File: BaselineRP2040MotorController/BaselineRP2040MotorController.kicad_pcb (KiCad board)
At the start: 2 copper layers, 133 parts, among them J2 Encoder 1, J3 Conn_01x03, J4 XT60 Power Connector, Q1 Q_PNP_BEC, Q2 Q_PNP_BEC, Q3 Q_PNP_BEC, U10 INA240A1D, U11 USBLC6-4SC6, U13 TX4139, U5 EG3113, U6 INA240A1D, U7 EG3113, U8 INA240A1D, U9 EG3113

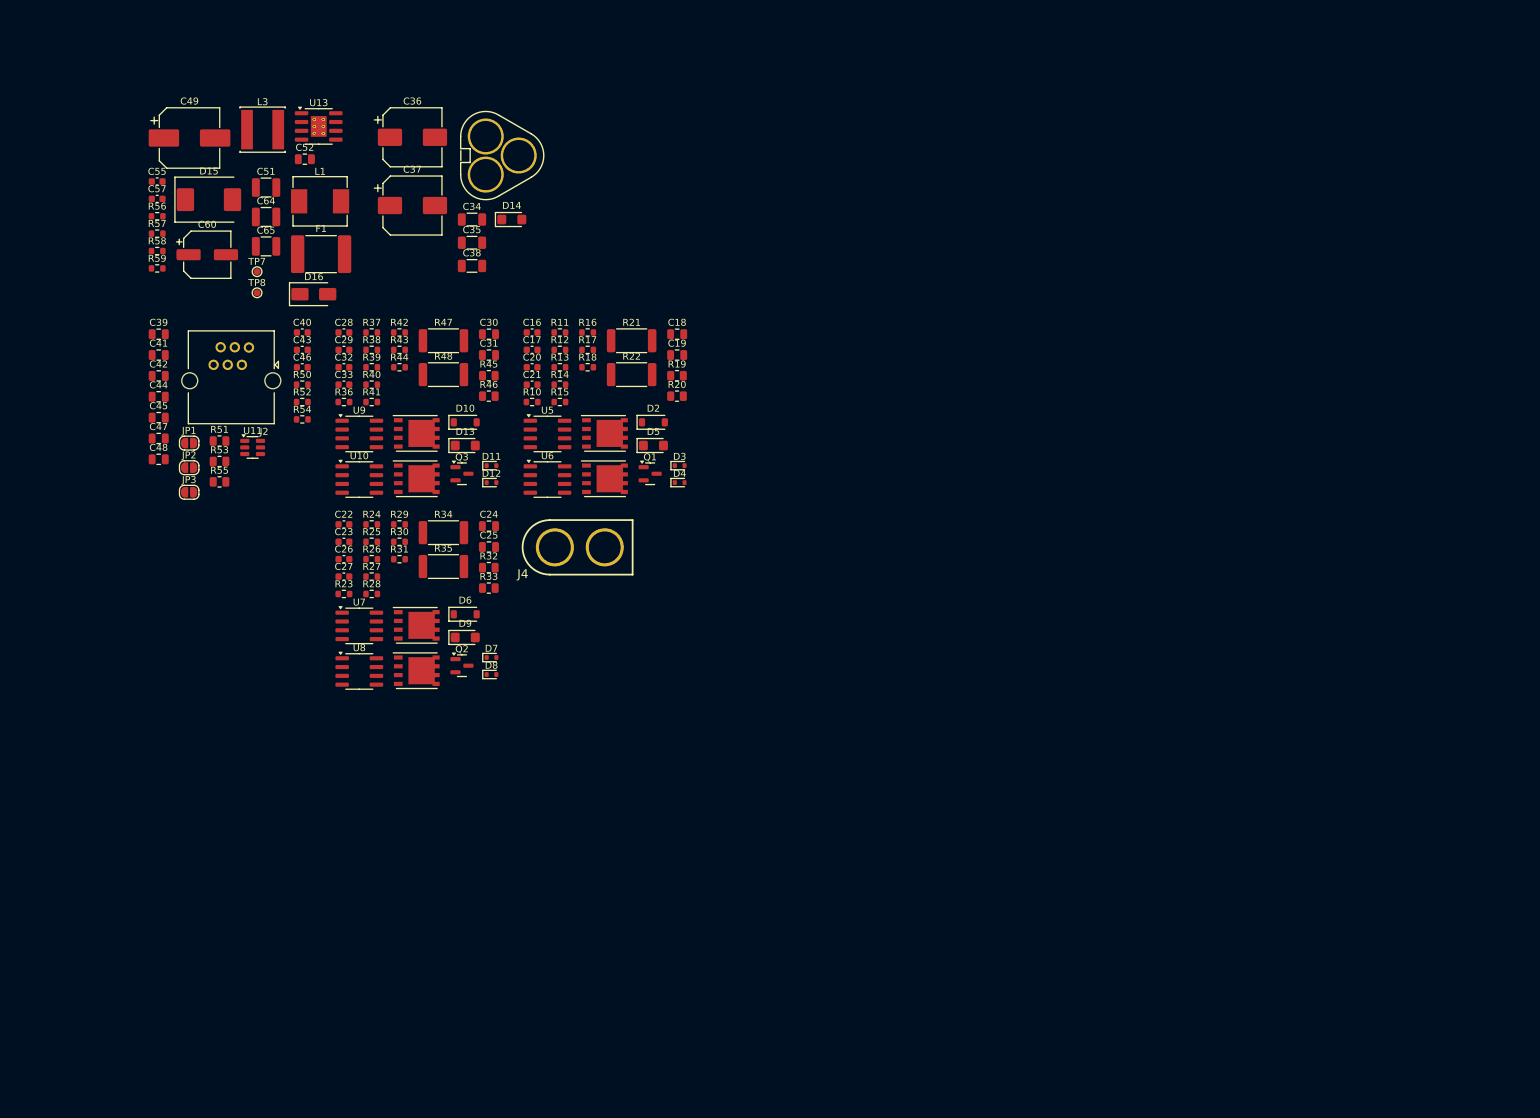
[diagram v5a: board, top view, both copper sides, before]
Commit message: Should have been a 4 layer board.
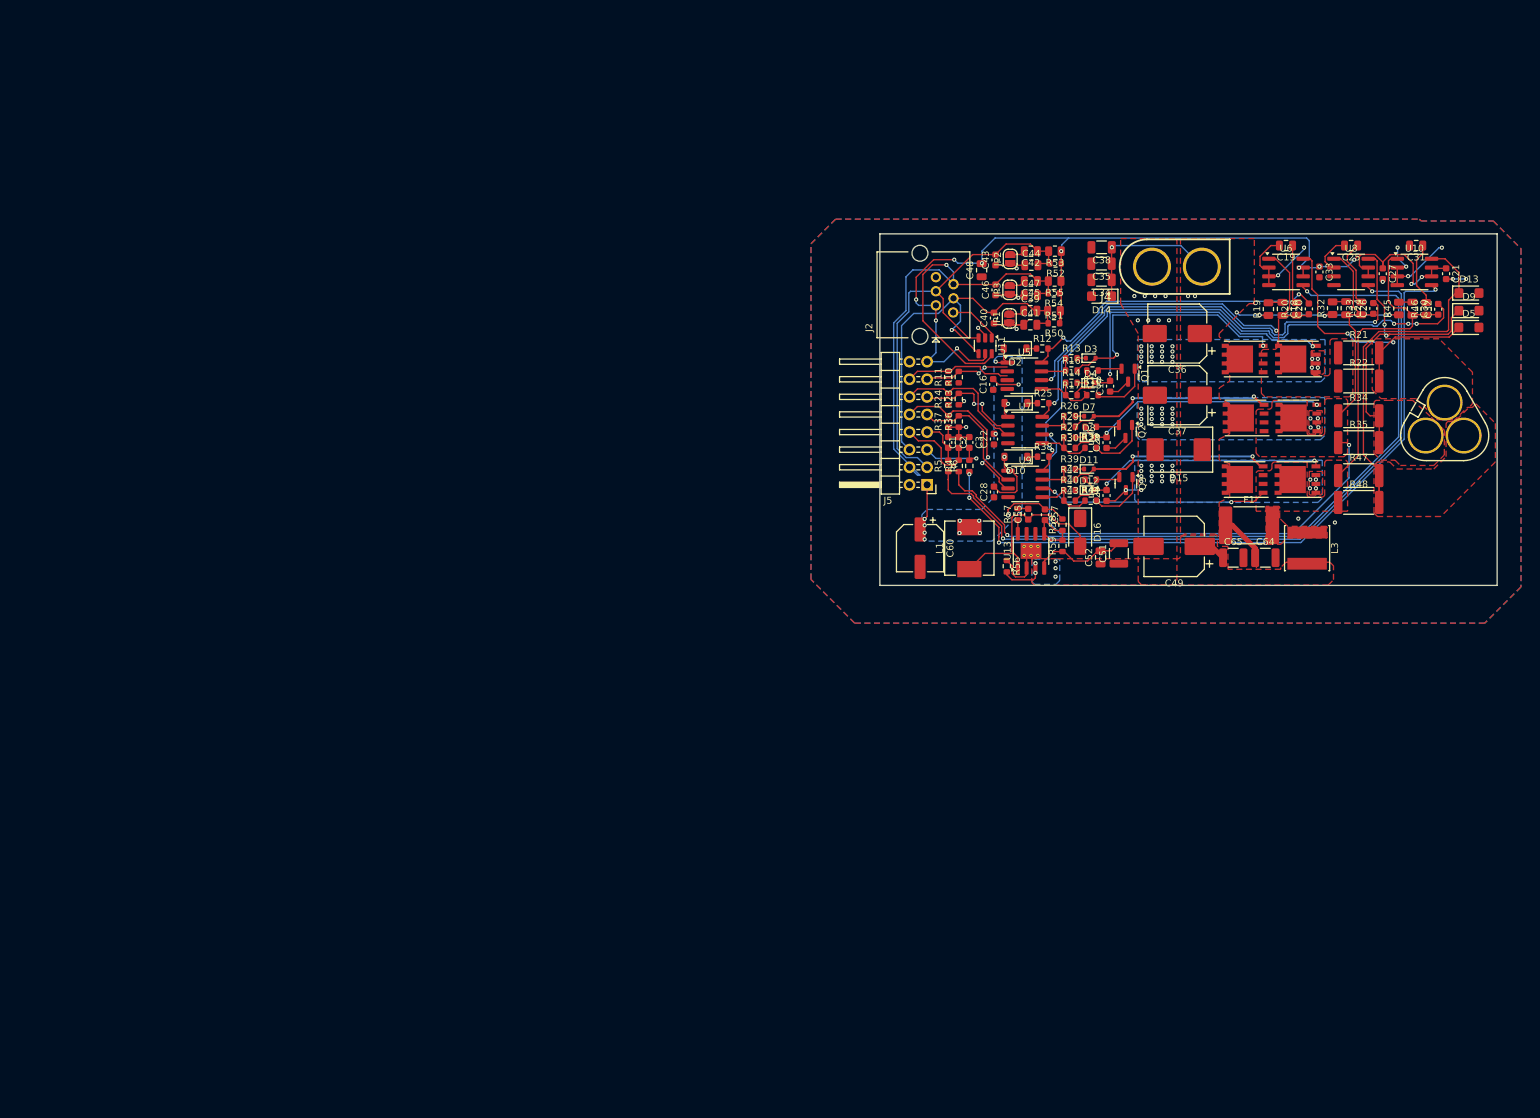
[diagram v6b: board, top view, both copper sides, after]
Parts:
- removed TP7, TP8: TestPoint, TestPoint:TestPoint_Pad_D1.0mm
- added C1: 0, Capacitor_SMD:C_0603_1608Metric, F.Cu at (161.8, 79.7)
- added C2: 0, Capacitor_SMD:C_0603_1608Metric, F.Cu at (160.3, 79.7)
- added C3: 0, Capacitor_SMD:C_0603_1608Metric, F.Cu at (163.3, 79.7)
- added J5: Conn_02x08_Odd_Even, Connector_PinHeader_2.54mm:PinHeader_2x08_P2.54mm_Horizontal, F.Cu at (157.2, 85.9)
- added R4: 0, Resistor_SMD:R_0603_1608Metric, F.Cu at (161.8, 83.1)
- added R5: 0, Resistor_SMD:R_0603_1608Metric, F.Cu at (160.3, 83.1)
- added R6: 0, Resistor_SMD:R_0603_1608Metric, F.Cu at (163.3, 83.1)
- J3: value Conn_01x03 -> 3 Pin XT30 / XT60
- moved L3 162.5 mm to (212.1, 95.0), turned to -90 degrees
- moved C32 158.2 mm to (231.0, 60.5), turned to 90 degrees
- moved C27 156.2 mm to (223.0, 55.4), turned to -90 degrees
- moved U10 155.3 mm to (227.6, 55.1)
- moved U8 154.4 mm to (218.4, 55.1)
- moved C49 153.9 mm to (192.9, 94.7), turned to 180 degrees
- moved C26 153.0 mm to (221.7, 60.4), turned to 90 degrees
- moved C64 152.4 mm to (206.1, 96.4)
- moved D9 152.4 mm to (235.5, 60.7)
- moved C65 146.7 mm to (201.4, 96.4)
- moved D13 146.6 mm to (235.5, 58.2)
- moved D15 144.6 mm to (193.5, 80.8), turned to 180 degrees
- moved J3 142.3 mm to (230.6, 76.4), turned to -30 degrees
- moved C33 141.8 mm to (213.9, 55.1), turned to -90 degrees
- moved F1 139.6 mm to (203.7, 91.7)
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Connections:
- net /BLDC Power Control/PWM_H_U renamed /PWM H U
- net /BLDC Power Control/PWM_H_V renamed /PWM H V
- net /BLDC Power Control/PWM_H_X renamed /PWM H X
- net /BLDC Power Control/PWM_L_U renamed /PWM L U
- net /BLDC Power Control/PWM_L_V renamed /PWM L V
- net /BLDC Power Control/PWM_L_X renamed /PWM L X
- AH1 pad 3: VMOT -> VMOT_PWR
- AH2 pad 3: VMOT -> VMOT_PWR
- AH3 pad 3: VMOT -> VMOT_PWR
- C34 pad 1: VMOT -> VMOT_PWR
- C35 pad 1: VMOT -> VMOT_PWR
- C36 pad 1: VMOT -> VMOT_PWR
- C37 pad 1: VMOT -> VMOT_PWR
- C38 pad 1: VMOT -> VMOT_PWR
- C64 pad 1: /Power Filtering/VMOT_RAW -> VMOT_PWR
- D14 pad 1: VMOT -> VMOT_PWR
- D15 pad 1: /Power Filtering/VMOT_RAW -> VMOT_PWR
- D16 pad 1: /Power Filtering/SW -> GND
- D16 pad 2: GND -> /Power Filtering/SW
- F1 pad 1: /Power Filtering/VMOT_RAW -> VMOT_PWR
- J4 pad 2: /Power Filtering/VMOT_RAW -> VMOT_PWR
- R19 pad 1: VMOT -> VMOT_PWR
- R32 pad 1: VMOT -> VMOT_PWR
- R45 pad 1: VMOT -> VMOT_PWR
- U10 pad 5: /BLDC Power Control/Motor Phase X/X_SENSE -> Net-(R6-Pad1)
- U13 pad 6: Net-(U13-EN) -> unconnected-(U13-EN-Pad6)
- U6 pad 5: /CurrentSense2 -> Net-(R4-Pad1)
- U8 pad 5: /CurrentSense1 -> Net-(R5-Pad1)
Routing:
- net +3V3: track 0.00 -> 142.3 mm, vias 0 -> 11
- net Net-(R4-Pad1): track 0.00 -> 110.0 mm, vias 0 -> 2
- net Net-(R5-Pad1): track 0.00 -> 104.7 mm, vias 0 -> 2
- net Net-(R6-Pad1): track 0.00 -> 103.4 mm, vias 0 -> 4
- net GND: track 0.00 -> 99.9 mm, vias 0 -> 87
- net /BLDC Power Control/Motor Phase V/A_P: track 0.00 -> 99.0 mm, vias 0 -> 2
- net /Encoder SCK: track 0.00 -> 86.4 mm, vias 0 -> 1
- net Net-(U9-VB): track 0.00 -> 83.1 mm, vias 0 -> 4
- net /BLDC Power Control/Motor Phase X/A_P: track 0.00 -> 79.9 mm, vias 0 -> 2
- net /Encoder CS: track 0.00 -> 65.9 mm
- net Net-(U7-VB): track 0.00 -> 65.7 mm, vias 0 -> 2
- net /BLDC Power Control/Motor Phase U/A_P: track 0.00 -> 59.7 mm, vias 0 -> 2
- net /Encoder RX: track 0.00 -> 57.3 mm, vias 0 -> 1
- net VMOT_PWR: track 0.00 -> 56.0 mm, vias 0 -> 7
- net /BLDC Power Control/Motor Phase X/A_N: track 0.00 -> 54.5 mm
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- added copper zone on B.Cu, net +12V
- added copper zone on F.Cu, net /BLDC Power Control/Motor Phase U/A_N
- added copper zone on F.Cu, net /BLDC Power Control/Motor Phase U/A_P
- added copper zone on F.Cu, net /BLDC Power Control/Motor Phase V/A_N
- added copper zone on F.Cu, net /BLDC Power Control/Motor Phase V/A_P
- added copper zone on F.Cu, net /BLDC Power Control/Motor Phase X/A_N
- added copper zone on F.Cu, net /BLDC Power Control/Motor Phase X/A_P
- added copper zone on B.Cu, net GND
- added copper zone on F.Cu, net GND
- added copper zone on F.Cu, net Net-(F1-Pad2)
- added copper zone on B.Cu, net VMOT
- added copper zone on F.Cu, net VMOT
- added copper zone on F.Cu, net VMOT_PWR
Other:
- board outline added: 89.1 x 50.8 mm

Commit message: Graphics.
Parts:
- added REF**: ESD-Logo_6.6x6mm_SilkScreen, Symbol:ESD-Logo_6.6x6mm_SilkScreen, F.Cu at (222.9, 93.6)
- added REF**: EastMakesLogo0.5x1CM, [EastMakes]BrandingLibrary:EastMakesLogo0.5x1CM, F.Cu at (228.5, 99.8)
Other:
- outline, holes or cut-outs redrawn
- board text added: "Any Machine is a Smoke Machine, If you use it wrong enough."
- board text added: "Do Not Make Finger Bacon"

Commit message: Mounting points
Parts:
- removed the REF** at (228.5, 99.8)
- added H1: MountingHole_Pad, MountingHole:MountingHole_3.2mm_M3_DIN965_Pad_TopBottom, F.Cu at (153.9, 103.6)
- added H2: MountingHole_Pad, MountingHole:MountingHole_3.2mm_M3_DIN965_Pad_TopBottom, F.Cu at (235.9, 103.6)
- added H3: MountingHole_Pad, MountingHole:MountingHole_3.2mm_M3_DIN965_Pad_TopBottom, F.Cu at (153.9, 46.9)
- added H4: MountingHole_Pad, MountingHole:MountingHole_3.2mm_M3_DIN965_Pad_TopBottom, F.Cu at (235.9, 46.9)
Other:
- board size 89.1 x 50.8 mm -> 88.5 x 63.2 mm
